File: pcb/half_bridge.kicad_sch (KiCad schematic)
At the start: 13 parts, among them Q1 IKW40N120H3, Q2 IKW40N120H3, U1 UCC21550BDWK

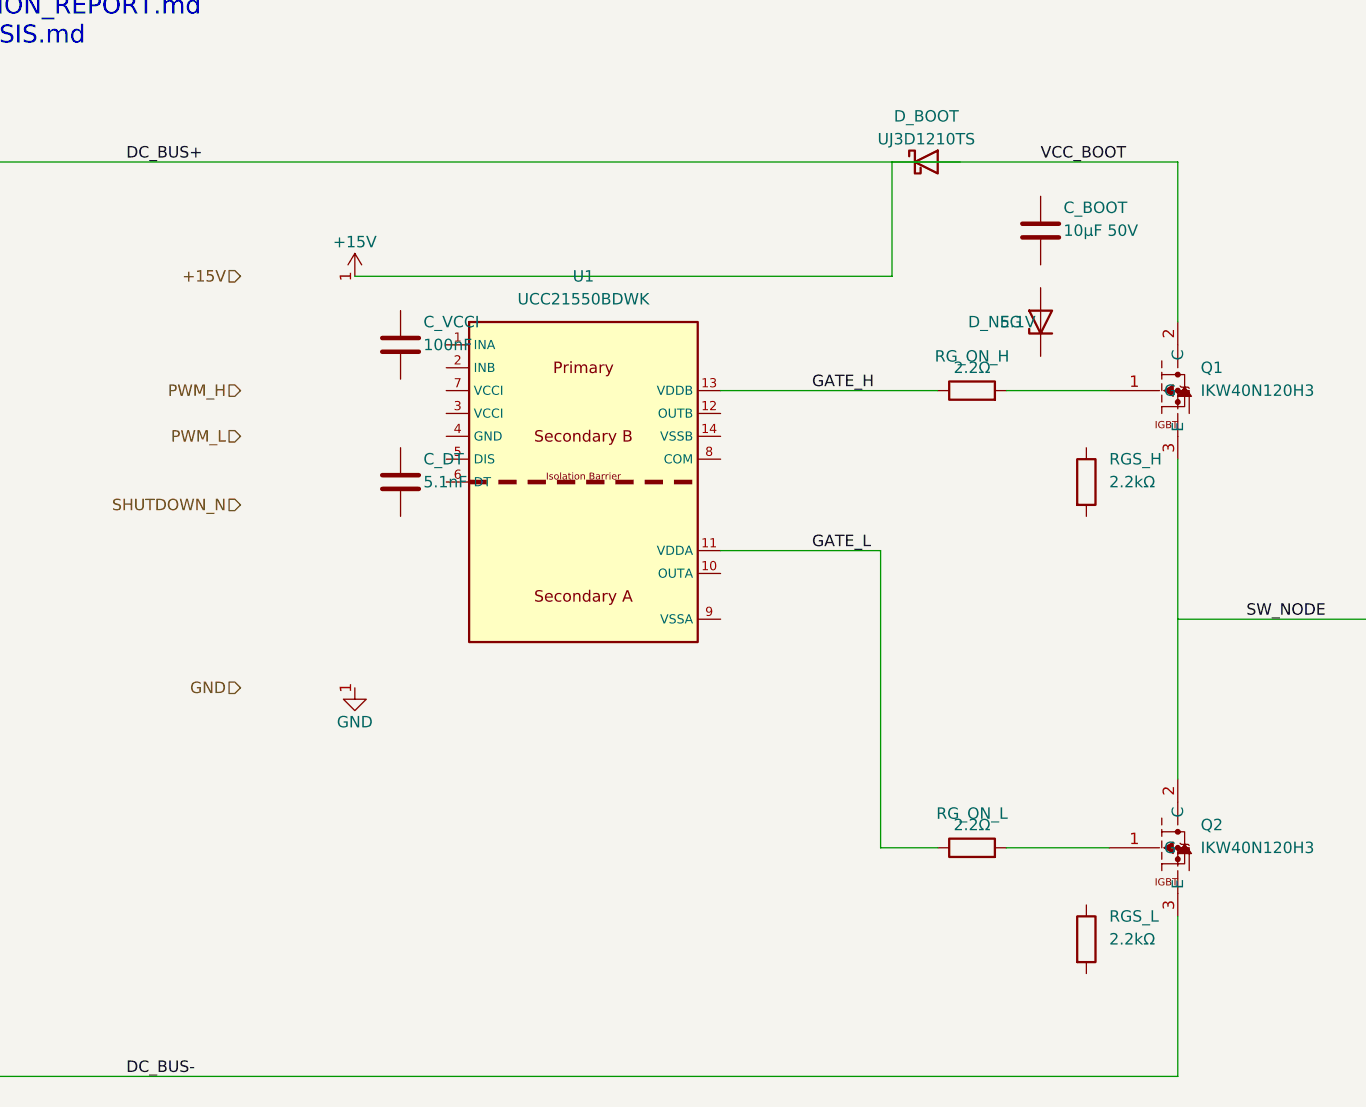
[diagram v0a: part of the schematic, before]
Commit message: fix: repair schematic wiring across all six PCB sheets
Systematic audit-and-verify pass over pcb/*.kicad_sch using a custom
union-find connectivity tracer, since KiCad's own ERC/netlist export only
confirm a file parses, not that intended nets are correct.

Found and fixed several serious latent bugs, none caught by prior tooling:
- mcu.kicad_sch: +3.3V shorted to two GPIOs; RTD_CS wired to the reset pin
  instead of a GPIO; all digital pins realigned to firmware/temper_pins.h
  after verifying firmware's pin choices against the real module symbol.
- half_bridge.kicad_sch: high-side IGBT wired backwards; bootstrap diode
  backwards; UCC21550 gate driver's entire control/supply side unwired.
- safety_interlock.kicad_sch: OCP comparator inputs swapped (inverted
  fault polarity); systematic wire-gap bug across comparators/logic gates;
  full NAND SR-latch rebuilt using real datasheet pin maps recovered from
  KiCad's own bundled multi-unit symbol libraries.
- power_management.kicad_sch: buck converter's SW pin was wired into the
  feedback divider instead of FB (coordinate typo); both ICs fully wired.
- power_input.kicad_sch: both mains rectifier diodes (D1, D2) in the
  voltage-doubler stage installed backwards, resolved via independent
  circuit-theory verification after design doc and atopile source
  disagreed with each other.
- sensing.kicad_sch: parse-blocking symbol bug; MAX31865 and ADUM1250
  fully wired (both were 100% unconnected).

user_interface.kicad_sch required no changes - confirmed already correct.

Documented the reusable techniques and root causes in docs/solutions/.

Co-Authored-By: Claude Sonnet 5 <noreply@anthropic.com>
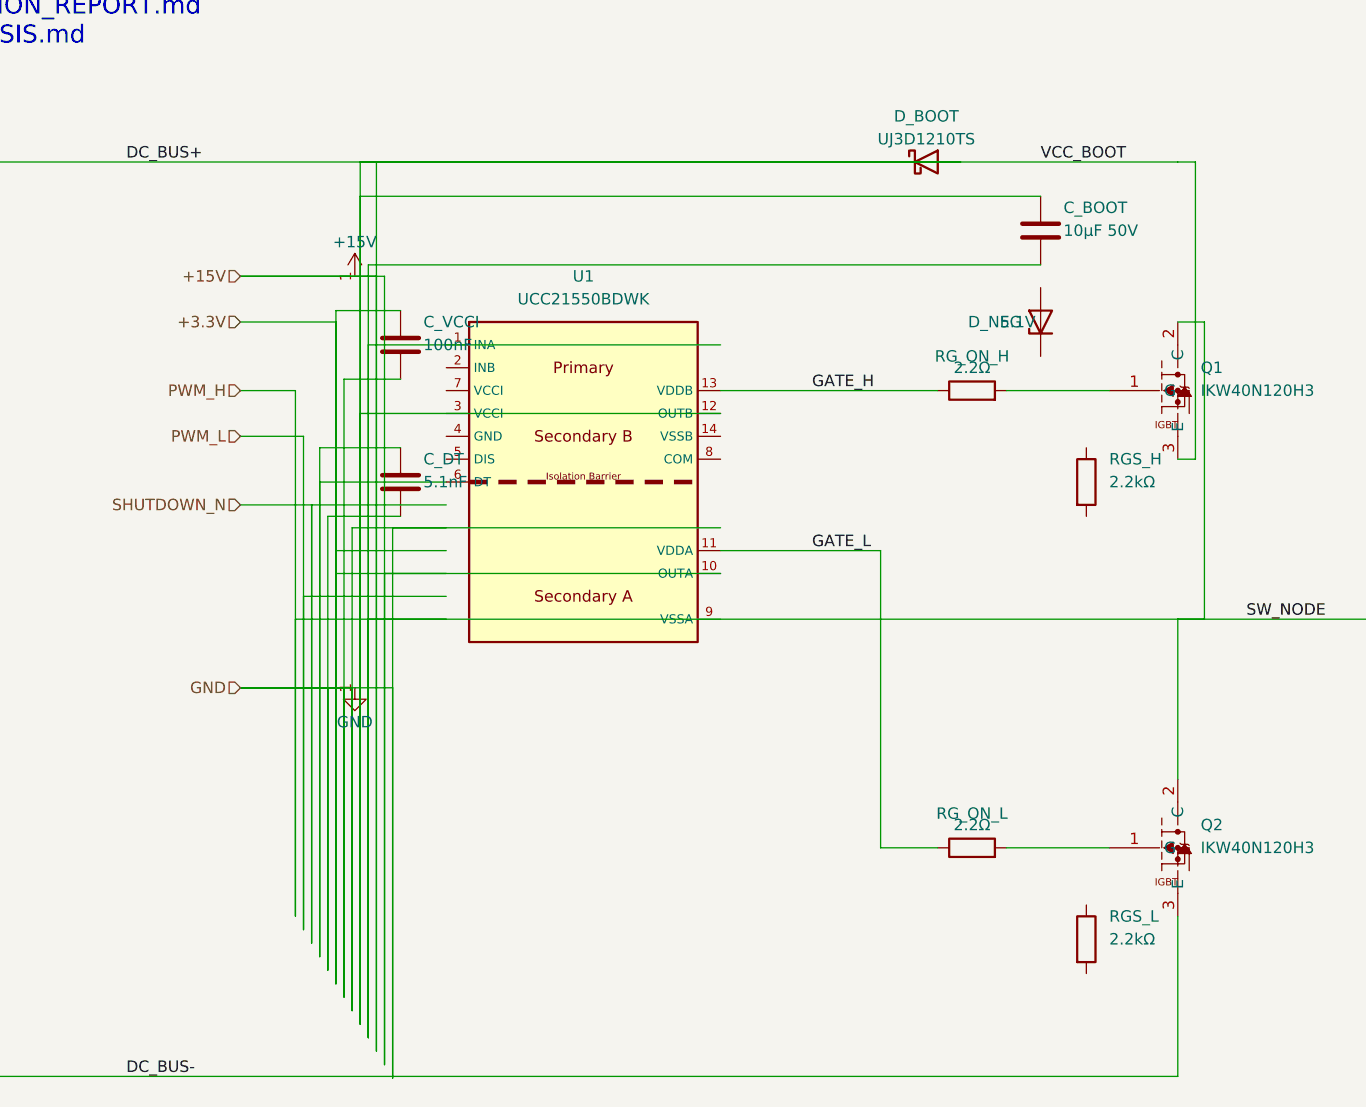
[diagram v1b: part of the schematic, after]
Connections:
- net DC_BUS+ is gone; now on net PWM_H: Q1.2 (C)
- net +15V: now also C_BOOT.1, C_VCCI.1, D_BOOT.2 (A), Q1.3 (E), U1.10 (OUTA), U1.12 (OUTB)
- net GND: now also C_DT.2, C_VCCI.2
- net PWM_H: now also C_BOOT.2, Q2.2 (C)
- net at U1.6 (DT): now also C_DT.1
- removed net SWITCH_NODE: Q1.3 (E), Q2.2 (C)
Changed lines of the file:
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@@
+    (effects (font (size 1.27 1.27)) (justify right))
+  )
+  (hierarchical_label "+3.3V"
+    (shape input)
+    (at 88.9 93.98 180)
+    (fields_autoplaced yes)
     (effects (font (size 1.27 1.27)) (justify right))
   )
@@
   )
   (wire
-    (pts (xy 193.04 76.2) (xy 193.04 93.98))
+    (pts (xy 193.04 76.2) (xy 195 76.2))
     (stroke (width 0) (type default))
     (uuid "wire-dcbus-plus-002")
   )
   (wire
-    (pts (xy 193.04 109.22) (xy 193.04 127))
+    (pts (xy 195 76.2) (xy 195 109.22))
+    (stroke (width 0) (type default))
+    (uuid "wire-dcbus-plus-002b")
+  )
+  (wire
+    (pts (xy 195 109.22) (xy 193.04 109.22))
+    (stroke (width 0) (type default))
+    (uuid "wire-dcbus-plus-002c")
+  )
+  (wire
+    (pts (xy 193.04 93.98) (xy 196 93.98))
     (stroke (width 0) (type default))
     (uuid "wire-swnode-001")
   )
   (wire
+    (pts (xy 196 93.98) (xy 196 127))
+    (stroke (width 0) (type default))
+    (uuid "wire-swnode-001b")
+  )
+  (wire
+    (pts (xy 196 127) (xy 193.04 127))
+    (stroke (width 0) (type default))
+    (uuid "wire-swnode-001c")
+  )
+  (wire
     (pts (xy 193.04 127) (xy 228.6 127))
     (stroke (width 0) (type default))
@@
     (stroke (width 0) (type default))
     (uuid "wire-dcbus-minus-002")
-  )
-  (wire
-    (pts (xy 101.6 88.9) (xy 161.29 88.9))
-    (stroke (width 0) (type default))
-    (uuid "wire-boot-supply-001")
-  )
-  (wire
-    (pts (xy 161.29 88.9) (xy 161.29 76.2))
-    (stroke (width 0) (type default))
-    (uuid "wire-boot-supply-002")
   )
   (wire
@@
     (uuid "label-gate-l-001")
   )
+  (wire (pts (xy 111.76 127.0) (xy 95.0 127.0)) (stroke (width 0) (type default)))
+  (wire (pts (xy 95.0 127.0) (xy 95.0 160.0)) (stroke (width 0) (type default)))
+  (wire (pts (xy 88.9 101.6) (xy 95.0 101.6)) (stroke (width 0) (type default)))
+  (wire (pts (xy 95.0 101.6) (xy 95.0 160.0)) (stroke (width 0) (type default)))
+  (wire (pts (xy 111.76 124.46) (xy 95.9 124.46)) (stroke (width 0) (type default)))
+  (wire (pts (xy 95.9 124.46) (xy 95.9 161.5)) (stroke (width 0) (type default)))
+  (wire (pts (xy 88.9 106.68) (xy 95.9 106.68)) (stroke (width 0) (type default)))
+  (wire (pts (xy 95.9 106.68) (xy 95.9 161.5)) (stroke (width 0) (type default)))
+  (wire (pts (xy 111.76 114.3) (xy 96.8 114.3)) (stroke (width 0) (type default)))
+  (wire (pts (xy 96.8 114.3) (xy 96.8 163.0)) (stroke (width 0) (type default)))
+  (wire (pts (xy 88.9 114.3) (xy 96.8 114.3)) (stroke (width 0) (type default)))
+  (wire (pts (xy 96.8 114.3) (xy 96.8 163.0)) (stroke (width 0) (type default)))
+  (wire (pts (xy 111.76 111.76) (xy 97.7 111.76)) (stroke (width 0) (type default)))
+  (wire (pts (xy 97.7 111.76) (xy 97.7 164.5)) (stroke (width 0) (type default)))
+  (wire (pts (xy 106.68 107.95) (xy 97.7 107.95)) (stroke (width 0) (type default)))
+  (wire (pts (xy 97.7 107.95) (xy 97.7 164.5)) (stroke (width 0) (type default)))
+  (wire (pts (xy 106.68 115.57) (xy 98.6 115.57)) (stroke (width 0) (type default)))
+  (wire (pts (xy 98.6 115.57) (xy 98.6 166.0)) (stroke (width 0) (type default)))
+  (wire (pts (xy 88.9 134.62) (xy 98.6 134.62)) (stroke (width 0) (type default)))
+  (wire (pts (xy 98.6 134.62) (xy 98.6 166.0)) (stroke (width 0) (type default)))
+  (wire (pts (xy 111.76 119.38) (xy 99.5 119.38)) (stroke (width 0) (type default)))
+  (wire (pts (xy 99.5 119.38) (xy 99.5 167.5)) (stroke (width 0) (type default)))
+  (wire (pts (xy 111.76 121.92) (xy 99.5 121.92)) (stroke (width 0) (type default)))
+  (wire (pts (xy 99.5 121.92) (xy 99.5 167.5)) (stroke (width 0) (type default)))
+  (wire (pts (xy 106.68 92.71) (xy 99.5 92.71)) (stroke (width 0) (type default)))
+  (wire (pts (xy 99.5 92.71) (xy 99.5 167.5)) (stroke (width 0) (type default)))
+  (wire (pts (xy 88.9 93.98) (xy 99.5 93.98)) (stroke (width 0) (type default)))
+  (wire (pts (xy 99.5 93.98) (xy 99.5 167.5)) (stroke (width 0) (type default)))
+  (wire (pts (xy 106.68 100.33) (xy 100.4 100.33)) (stroke (width 0) (type default)))
+  (wire (pts (xy 100.4 100.33) (xy 100.4 169.0)) (stroke (width 0) (type default)))
+  (wire (pts (xy 88.9 134.62) (xy 100.4 134.62)) (stroke (width 0) (type default)))
+  (wire (pts (xy 100.4 134.62) (xy 100.4 169.0)) (stroke (width 0) (type default)))
+  (wire (pts (xy 111.76 116.84) (xy 101.3 116.84)) (stroke (width 0) (type default)))
+  (wire (pts (xy 101.3 116.84) (xy 101.3 170.5)) (stroke (width 0) (type default)))
+  (wire (pts (xy 88.9 134.62) (xy 101.3 134.62)) (stroke (width 0) (type default)))
+  (wire (pts (xy 101.3 134.62) (xy 101.3 170.5)) (stroke (width 0) (type default)))
+  (wire (pts (xy 142.24 104.14) (xy 102.2 104.14)) (stroke (width 0) (type default)))
+  (wire (pts (xy 102.2 104.14) (xy 102.2 172.0)) (stroke (width 0) (type default)))
+  (wire (pts (xy 161.29 76.2) (xy 102.2 76.2)) (stroke (width 0) (type default)))
+  (wire (pts (xy 102.2 76.2) (xy 102.2 172.0)) (stroke (width 0) (type default)))
+  (wire (pts (xy 177.8 80.01) (xy 102.2 80.01)) (stroke (width 0) (type default)))
+  (wire (pts (xy 102.2 80.01) (xy 102.2 172.0)) (stroke (width 0) (type default)))
+  (wire (pts (xy 142.24 96.52) (xy 103.1 96.52)) (stroke (width 0) (type default)))
+  (wire (pts (xy 103.1 96.52) (xy 103.1 173.5)) (stroke (width 0) (type default)))
+  (wire (pts (xy 177.8 87.63) (xy 103.1 87.63)) (stroke (width 0) (type default)))
+  (wire (pts (xy 103.1 87.63) (xy 103.1 173.5)) (stroke (width 0) (type default)))
+  (wire (pts (xy 193.04 127.0) (xy 103.1 127.0)) (stroke (width 0) (type default)))
+  (wire (pts (xy 103.1 127.0) (xy 103.1 173.5)) (stroke (width 0) (type default)))
+  (wire (pts (xy 168.91 76.2) (xy 104.0 76.2)) (stroke (width 0) (type default)))
+  (wire (pts (xy 104.0 76.2) (xy 104.0 175.0)) (stroke (width 0) (type default)))
+  (wire (pts (xy 88.9 88.9) (xy 104.0 88.9)) (stroke (width 0) (type default)))
+  (wire (pts (xy 104.0 88.9) (xy 104.0 175.0)) (stroke (width 0) (type default)))
+  (wire (pts (xy 142.24 121.92) (xy 104.9 121.92)) (stroke (width 0) (type default)))
+  (wire (pts (xy 104.9 121.92) (xy 104.9 176.5)) (stroke (width 0) (type default)))
+  (wire (pts (xy 88.9 88.9) (xy 104.9 88.9)) (stroke (width 0) (type default)))
+  (wire (pts (xy 104.9 88.9) (xy 104.9 176.5)) (stroke (width 0) (type default)))
+  (wire (pts (xy 142.24 116.84) (xy 105.8 116.84)) (stroke (width 0) (type default)))
+  (wire (pts (xy 105.8 116.84) (xy 105.8 178.0)) (stroke (width 0) (type default)))
+  (wire (pts (xy 88.9 134.62) (xy 105.8 134.62)) (stroke (width 0) (type default)))
+  (wire (pts (xy 105.8 134.62) (xy 105.8 178.0)) (stroke (width 0) (type default)))
 )

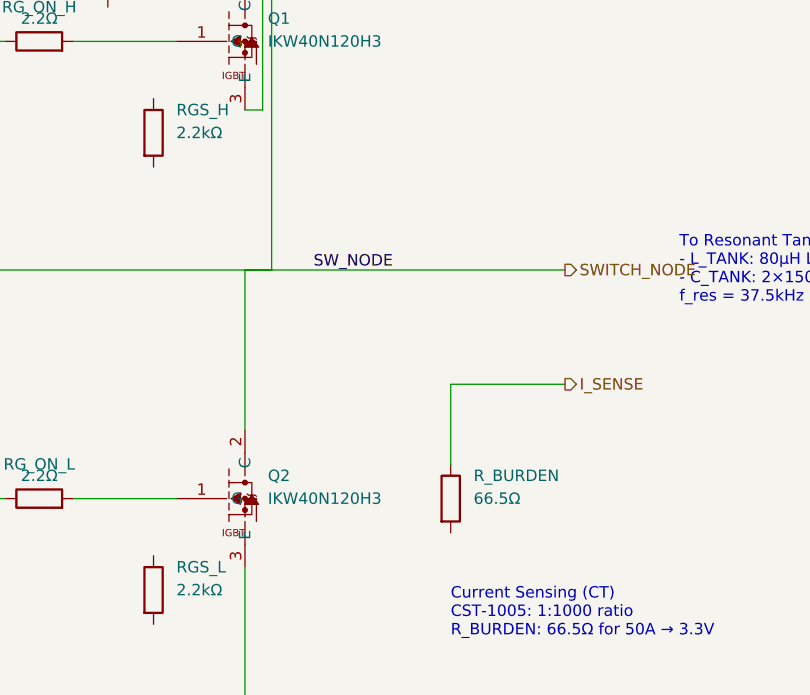
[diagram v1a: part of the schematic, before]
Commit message: fix: remediate 8 remaining open schematic items (relay driver, R_BURDEN dedup, MAX31865 footprint, isolated 5V, RUNAWAY_CUT/RESET_N, fault-LED taps)
Closes out the open-questions list from the prior schematic repair session
(docs/plans/2026-07-14-001-fix-schematic-open-items-remediation-plan.md):

- Fix AC_N routing to the doubler's center tap (independently re-derived via
  KCL before editing mains wiring), in both the schematic and elec/src
- Give GND_CENTER a real ground connection and a Y2-capacitor PE bond;
  resolved a real conflict between two hardware docs on where system
  ground lives, using the generative .ato source as an independent tiebreaker
- Add the NTC bypass relay + low-side MOSFET driver circuit for RELAY_CTRL
- Consolidate duplicate R_BURDEN into Half_Bridge; found the surviving
  copy's signal/reference pins were swapped
- Fix the MAX31865 footprint (wrong package entirely) and add the missing
  pcb/fp-lib-table
- Add the isolated +5V_ISO DC-DC supply for the I2C isolator's far side
- Remove vestigial MCU_ENABLE; wire the real RUNAWAY_CUT net using the
  74HC4075's actual datasheet-sourced gate mapping, not pin-adjacency guesses
- Fix User_Interface's stale root pins and hierarchize the four fault-LED
  taps in Safety_Interlock (all four were floating, not just WDT_FAULT)

Every unit verified via union-find connectivity trace before and after
writing, plus a full-project kicad-cli parse/ERC pass. Three bugs were
self-caught by that discipline before landing: a lib_symbols block placed
outside its container (broke the parser outright), a RESET_N direction
mismatch, and a shared-sheet-edge routing overlap -- the latter two folded
into docs/solutions/tooling-decisions/kicad-schematic-connectivity-tracer.

Co-Authored-By: Claude Sonnet 5 <noreply@anthropic.com>
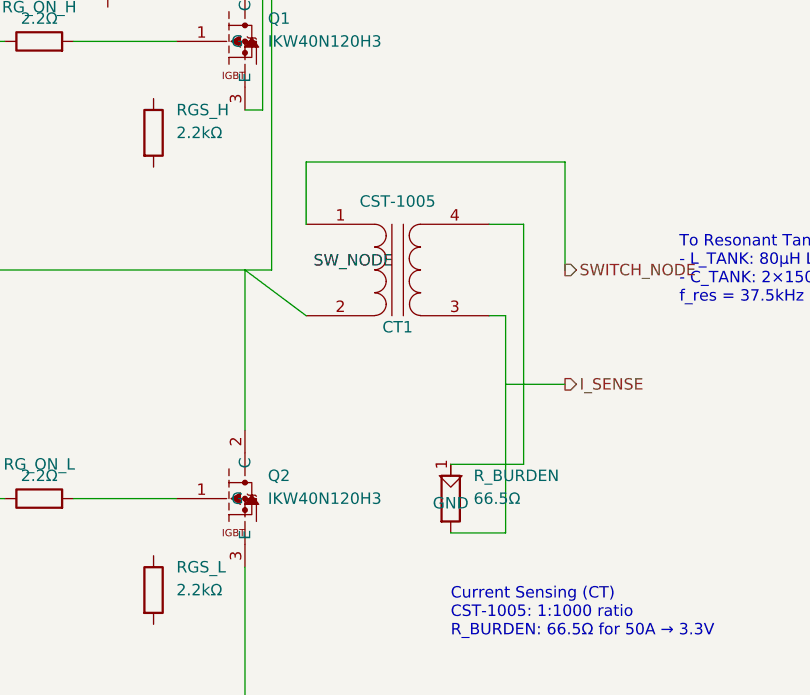
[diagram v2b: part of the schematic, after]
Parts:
- added CT1: CST-1005, CST1005_Footprint, symbol Device:Transformer_1P_1S
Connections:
- net GND: now also R_BURDEN.1, CT1.4 (SB)
- net I_SENSE: now also R_BURDEN.2, CT1.3 (SA); no longer R_BURDEN.1
- net PWM_H: now also CT1.2 (AB)
- new net SWITCH_NODE: CT1.1 (AA)
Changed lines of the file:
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@@
     (pin "2" (uuid "cdt-pin2-uuid"))
+  )
+  (symbol
+    (lib_id "Device:Transformer_1P_1S")
+    (at 210.0 127.0 0)
+    (unit 1)
+    (exclude_from_sim no)
+    (in_bom yes)
+    (on_board yes)
+    (dnp no)
+    (property "Reference" "CT1" (at 210.0 133.35 0) (effects (font (size 1.27 1.27))))
+    (property "Value" "CST-1005" (at 210.0 119.38 0) (effects (font (size 1.27 1.27))))
+    (property "Footprint" "CST1005_Footprint" (at 210.0 127.0 0) (effects (font (size 1.27 1.27)) hide))
+    (property "MPN" "CST-1005" (at 210.0 127.0 0) (effects (font (size 1.27 1.27)) hide))
+    (property "Description" "Current transformer 1:1000, primary threaded in series with SWITCH_NODE/tank current, secondary across R_BURDEN" (at 210.0 127.0 0) (effects (font (size 1.27 1.27)) hide))
+    (pin "1" (uuid "ct1-pin1-uuid"))
+    (pin "2" (uuid "ct1-pin2-uuid"))
+    (pin "3" (uuid "ct1-pin3-uuid"))
+    (pin "4" (uuid "ct1-pin4-uuid"))
+  )
+  (symbol
+    (lib_id "power:GND")
+    (at 215.9 148.59 0)
+    (unit 1)
+    (exclude_from_sim no)
+    (in_bom no)
+    (on_board no)
+    (property "Reference" "#PWR05" (at 215.9 154.432 0) (effects (font (size 1.27 1.27)) hide))
+    (property "Value" "GND" (at 215.9 152.908 0) (effects (font (size 1.27 1.27))))
   )
   (text "Current Sensing (CT)\nCST-1005: 1:1000 ratio\nR_BURDEN: 66.5Ω for 50A → 3.3V"
@@
   )
   (wire
-    (pts (xy 193.04 127) (xy 228.6 127))
+    (pts (xy 193.04 127) (xy 199.84 132.08))
     (stroke (width 0) (type default))
     (uuid "wire-swnode-002")
+  )
+  (wire
+    (pts (xy 199.84 121.92) (xy 199.84 115.0))
+    (stroke (width 0) (type default))
+    (uuid "wire-ct-primary-001")
+  )
+  (wire
+    (pts (xy 199.84 115.0) (xy 228.6 115.0))
+    (stroke (width 0) (type default))
+    (uuid "wire-ct-primary-002")
+  )
+  (wire
+    (pts (xy 228.6 115.0) (xy 228.6 127.0))
+    (stroke (width 0) (type default))
+    (uuid "wire-ct-primary-003")
   )
   (wire
@@
   )
   (wire
-    (pts (xy 215.9 139.7) (xy 228.6 139.7))
+    (pts (xy 215.9 156.21) (xy 222.0 156.21))
     (stroke (width 0) (type default))
     (uuid "wire-isense-001")
   )
   (wire
-    (pts (xy 215.9 148.59) (xy 215.9 139.7))
+    (pts (xy 222.0 156.21) (xy 222.0 139.7))
     (stroke (width 0) (type default))
     (uuid "wire-isense-002")
   )
+  (wire
+    (pts (xy 222.0 139.7) (xy 228.6 139.7))
+    (stroke (width 0) (type default))
+    (uuid "wire-isense-003")
+  )
+  (wire
+    (pts (xy 220.16 132.08) (xy 222.0 132.08))
+    (stroke (width 0) (type default))
+    (uuid "wire-isense-004")
+  )
+  (wire
+    (pts (xy 222.0 132.08) (xy 222.0 139.7))
+    (stroke (width 0) (type default))
+    (uuid "wire-isense-005")
+  )
+  (wire
+    (pts (xy 220.16 121.92) (xy 224.0 121.92))
+    (stroke (width 0) (type default))
+    (uuid "wire-isense-ref-001")
+  )
+  (wire
+    (pts (xy 224.0 121.92) (xy 224.0 148.59))
+    (stroke (width 0) (type default))
+    (uuid "wire-isense-ref-002")
+  )
+  (wire
+    (pts (xy 224.0 148.59) (xy 215.9 148.59))
+    (stroke (width 0) (type default))
+    (uuid "wire-isense-ref-003")
+  )
   (label "DC_BUS+"
